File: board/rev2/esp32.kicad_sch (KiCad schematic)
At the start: 3 parts, among them U7 ESP32-C6-WROOM-1

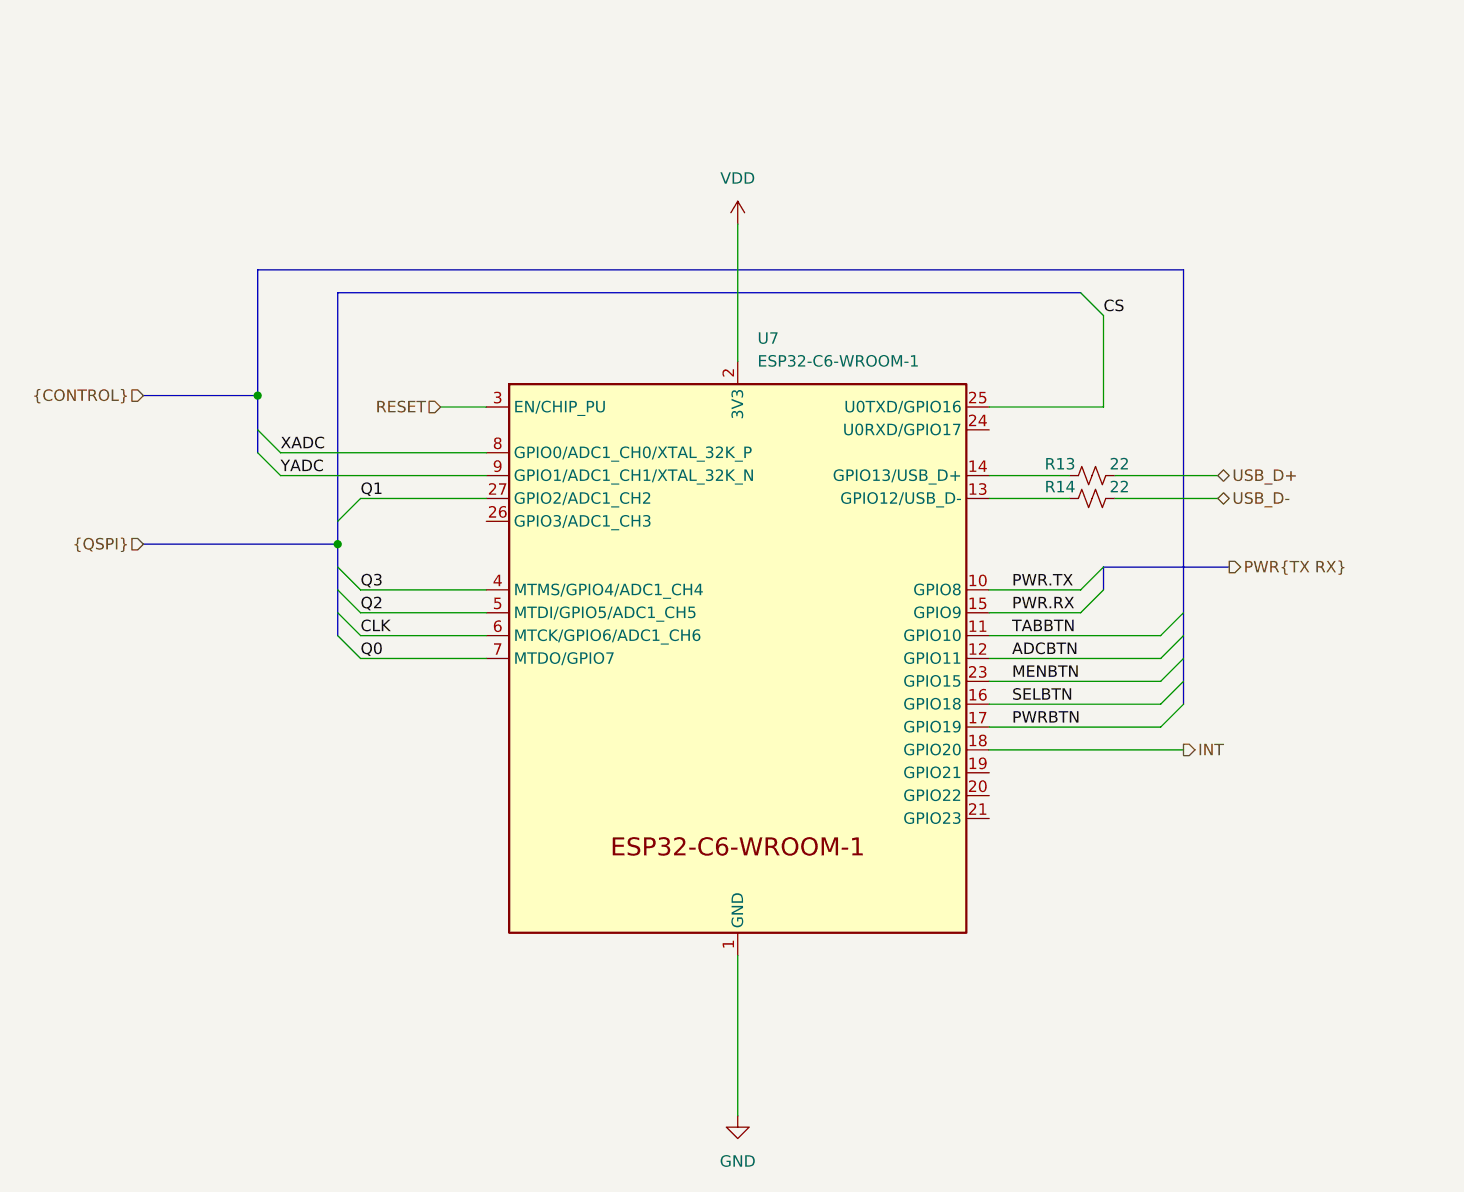
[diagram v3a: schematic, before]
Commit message: Add netclasses, more footprints, fix ERC
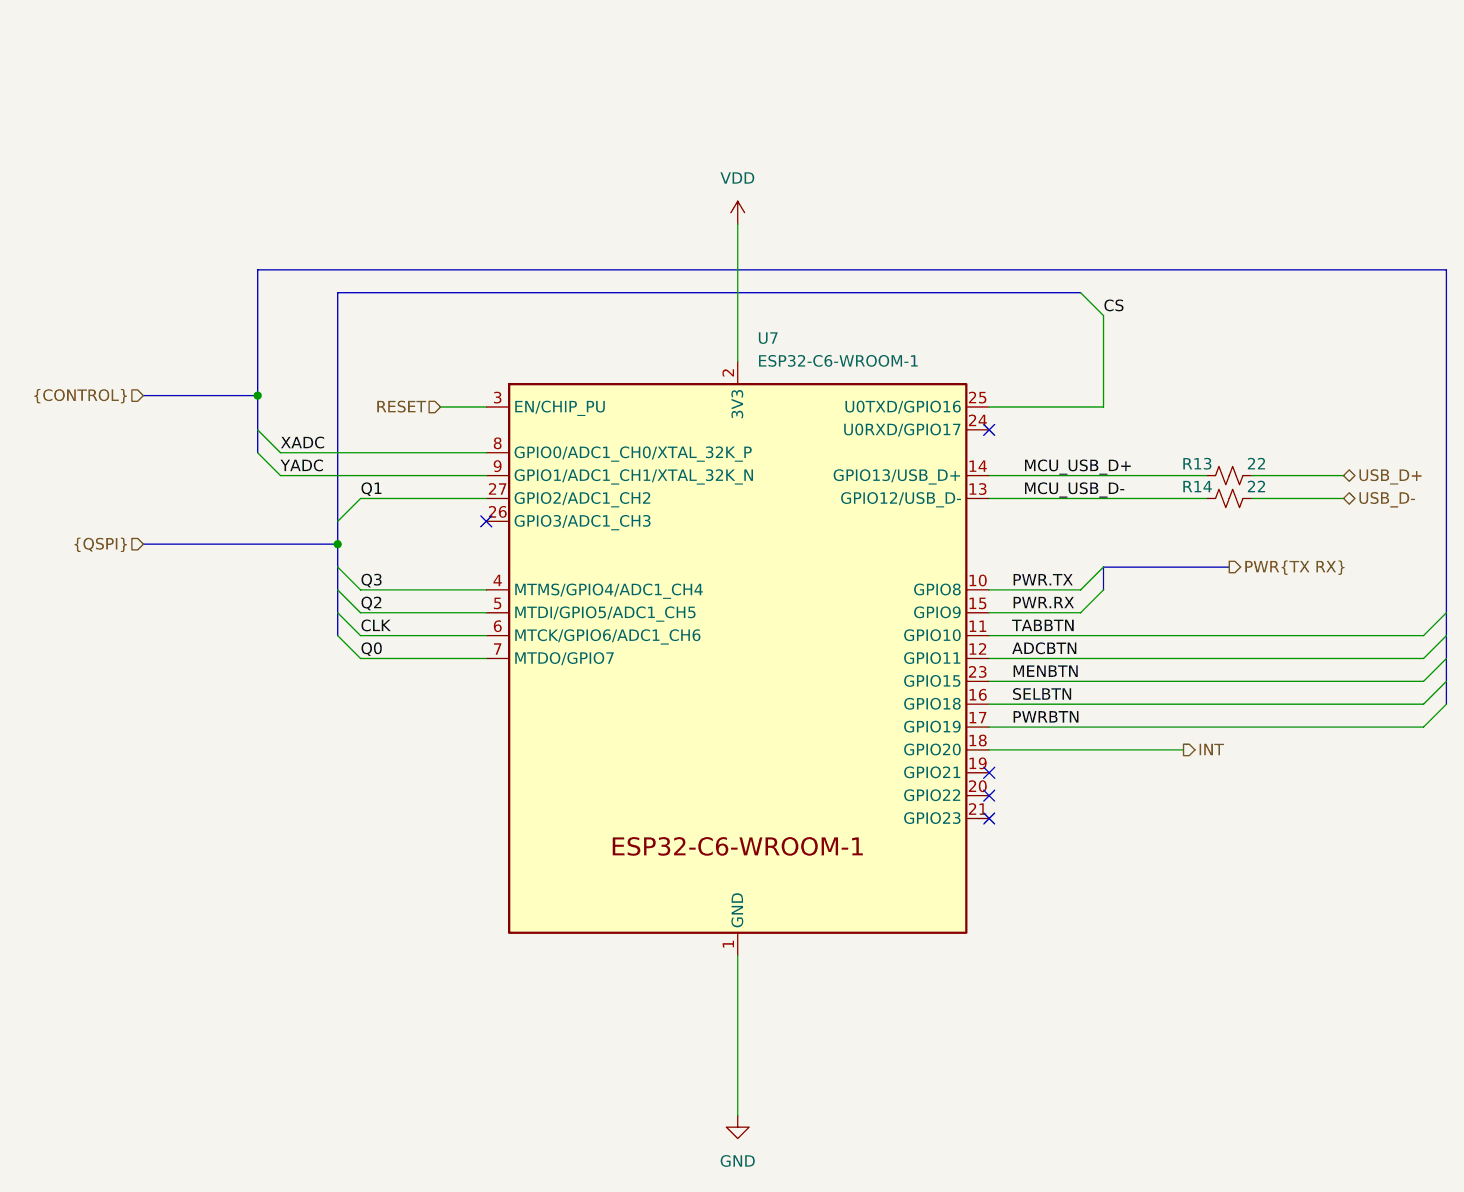
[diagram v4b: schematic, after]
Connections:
- net MCU_USB_D-: now reaches R14.1, U7.13 (GPIO12/USB_D-)
- net MCU_USB_D+: now reaches R13.1, U7.14 (GPIO13/USB_D+)
- no-connect marks 0 -> 5
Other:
- moved on the sheet: R13, R14
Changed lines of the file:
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@@
 		(color 0 0 0 0)
 	)
-	(bus_entry
-		(at 187.96 97.79)
+	(no_connect
+		(at 166.37 67.31)
+	)
+	(no_connect
+		(at 166.37 107.95)
+	)
+	(no_connect
+		(at 166.37 110.49)
+	)
+	(no_connect
+		(at 110.49 77.47)
+	)
+	(no_connect
+		(at 166.37 105.41)
+	)
+	(bus_entry
+		(at 217.17 97.79)
 		(size -2.54 2.54)
 		(stroke
@@
 	)
 	(bus_entry
-		(at 187.96 87.63)
+		(at 217.17 87.63)
 		(size -2.54 2.54)
 		(stroke
@@
 	)
 	(bus_entry
-		(at 187.96 90.17)
+		(at 217.17 90.17)
 		(size -2.54 2.54)
 		(stroke
@@
 	)
 	(bus_entry
-		(at 187.96 95.25)
+		(at 217.17 95.25)
 		(size -2.54 2.54)
 		(stroke
@@
 	)
 	(bus_entry
-		(at 187.96 92.71)
+		(at 217.17 92.71)
 		(size -2.54 2.54)
 		(stroke
@@
 	(wire
 		(pts
-			(xy 166.37 97.79) (xy 185.42 97.79)
+			(xy 166.37 97.79) (xy 214.63 97.79)
 		)
 		(stroke
@@
 	(bus
 		(pts
-			(xy 187.96 95.25) (xy 187.96 97.79)
+			(xy 217.17 95.25) (xy 217.17 97.79)
 		)
 		(stroke
@@
 	(wire
 		(pts
-			(xy 166.37 100.33) (xy 185.42 100.33)
+			(xy 166.37 100.33) (xy 214.63 100.33)
 		)
 		(stroke
@@
 	(wire
 		(pts
-			(xy 166.37 95.25) (xy 185.42 95.25)
-		)
-		(stroke
-			(width 0)
-			(type default)
-		)
-	)
-	(wire
-		(pts
-			(xy 166.37 90.17) (xy 185.42 90.17)
+			(xy 166.37 95.25) (xy 214.63 95.25)
+		)
+		(stroke
+			(width 0)
+			(type default)
+		)
+	)
+	(wire
+		(pts
+			(xy 166.37 90.17) (xy 214.63 90.17)
 		)
 		(stroke
@@
 	(bus
 		(pts
-			(xy 187.96 90.17) (xy 187.96 92.71)
+			(xy 217.17 90.17) (xy 217.17 92.71)
 		)
 		(stroke
@@
 	(wire
 		(pts
-			(xy 166.37 92.71) (xy 185.42 92.71)
-		)
-		(stroke
-			(width 0)
-			(type default)
-		)
-	)
-	(wire
-		(pts
-			(xy 180.34 72.39) (xy 191.77 72.39)
-		)
-		(stroke
-			(width 0)
-			(type default)
-		)
-	)
-	(bus
-		(pts
-			(xy 187.96 87.63) (xy 187.96 90.17)
+			(xy 166.37 92.71) (xy 214.63 92.71)
+		)
+		(stroke
+			(width 0)
+			(type default)
+		)
+	)
+	(wire
+		(pts
+			(xy 195.58 72.39) (xy 205.74 72.39)
+		)
+		(stroke
+			(width 0)
+			(type default)
+		)
+	)
+	(bus
+		(pts
+			(xy 217.17 87.63) (xy 217.17 90.17)
 		)
 		(stroke
@@
 	(bus
 		(pts
-			(xy 187.96 92.71) (xy 187.96 95.25)
+			(xy 217.17 92.71) (xy 217.17 95.25)
 		)
 		(stroke
@@
 	(wire
 		(pts
-			(xy 166.37 72.39) (xy 175.26 72.39)
-		)
-		(stroke
-			(width 0)
-			(type default)
-		)
-	)
-	(bus
-		(pts
-			(xy 85.09 49.53) (xy 187.96 49.53)
-		)
-		(stroke
-			(width 0)
-			(type default)
-		)
-	)
-	(wire
-		(pts
-			(xy 166.37 74.93) (xy 175.26 74.93)
+			(xy 166.37 72.39) (xy 190.5 72.39)
+		)
+		(stroke
+			(width 0)
+			(type default)
+		)
+	)
+	(bus
+		(pts
+			(xy 85.09 49.53) (xy 217.17 49.53)
+		)
+		(stroke
+			(width 0)
+			(type default)
+		)
+	)
+	(wire
+		(pts
+			(xy 166.37 74.93) (xy 190.5 74.93)
 		)
 		(stroke
@@
 	(bus
 		(pts
-			(xy 187.96 49.53) (xy 187.96 87.63)
+			(xy 217.17 49.53) (xy 217.17 87.63)
 		)
 		(stroke
@@
 	(wire
 		(pts
-			(xy 180.34 74.93) (xy 191.77 74.93)
+			(xy 195.58 74.93) (xy 205.74 74.93)
 		)
 		(stroke
@@
 		)
 	)
+	(label "MCU_USB_D+"
+		(at 170.18 72.39 0)
+		(effects
+			(font
+				(size 1.27 1.27)
+			)
+			(justify left bottom)
+		)
+	)
+	(label "MCU_USB_D-"
+		(at 170.18 74.93 0)
+		(effects
+			(font
+				(size 1.27 1.27)
+			)
+			(justify left bottom)
+		)
+	)
 	(label "Q2"
 		(at 96.52 87.63 0)
@@
 	(hierarchical_label "USB_D+"
 		(shape bidirectional)
-		(at 191.77 72.39 0)
+		(at 205.74 72.39 0)
 		(effects
 			(font
@@
 	(hierarchical_label "USB_D-"
 		(shape bidirectional)
-		(at 191.77 74.93 0)
+		(at 205.74 74.93 0)
 		(effects
 			(font
@@
 			)
 			(justify right)
+		)
+	)
+	(rule_area
+		(polyline
+			(pts
+				(xy 168.91 68.58) (xy 201.93 68.58) (xy 201.93 77.47) (xy 168.91 77.47)
+			)
+			(stroke
+				(width 0)
+				(type dash)
+			)
+			(fill
+				(type none)
+			)
+		)
+	)
+	(netclass_flag ""
+		(length 2.54)
+		(shape round)
+		(at 187.96 68.58 0)
+		(fields_autoplaced yes)
+		(effects
+			(font
+				(size 1.27 1.27)
+			)
+			(justify left bottom)
+		)
+		(property "Netclass" "USB"
+			(at 188.6585 66.04 0)
+			(effects
+				(font
+					(size 1.27 1.27)
+				)
+				(justify left)
+			)
+		)
+		(property "Component Class" ""
+			(at -34.29 -2.54 0)
+			(effects
+				(font
+					(size 1.27 1.27)
+					(italic yes)
+				)
+			)
 		)
 	)
@@
 	(symbol
 		(lib_id "Device:R_Small_US")
-		(at 177.8 74.93 90)
+		(at 193.04 74.93 90)
 		(unit 1)
 		(exclude_from_sim no)
@@
 		(dnp no)
 		(property "Reference" "R14"
-			(at 174.244 73.66 90)
+			(at 189.484 73.66 90)
 			(effects
 				(font
@@
 		)
 		(property "Value" "22"
-			(at 180.848 73.66 90)
+			(at 196.088 73.66 90)
 			(effects
 				(font
@@
 		)
 		(property "Footprint" "Resistor_SMD:R_0402_1005Metric"
-			(at 177.8 74.93 0)
+			(at 193.04 74.93 0)
 			(effects
 				(font
@@
 		)
 		(property "Datasheet" "~"
-			(at 177.8 74.93 0)
+			(at 193.04 74.93 0)
 			(effects
 				(font
@@
 		)
 		(property "Description" "Resistor, small US symbol"
-			(at 177.8 74.93 0)
+			(at 193.04 74.93 0)
 			(effects
 				(font
@@
 		)
 		(property "Part" " 0402WGF220JTCE"
-			(at 177.8 74.93 90)
+			(at 193.04 74.93 90)
 			(effects
 				(font
@@
 	(symbol
 		(lib_id "Device:R_Small_US")
-		(at 177.8 72.39 90)
+		(at 193.04 72.39 90)
 		(unit 1)
 		(exclude_from_sim no)
@@
 		(dnp no)
 		(property "Reference" "R13"
-			(at 174.244 71.12 90)
+			(at 189.484 71.12 90)
 			(effects
 				(font
@@
 		)
 		(property "Value" "22"
-			(at 180.848 71.12 90)
+			(at 196.088 71.12 90)
 			(effects
 				(font
@@
 		)
 		(property "Footprint" "Resistor_SMD:R_0402_1005Metric"
-			(at 177.8 72.39 0)
+			(at 193.04 72.39 0)
 			(effects
 				(font
@@
 		)
 		(property "Datasheet" "~"
-			(at 177.8 72.39 0)
+			(at 193.04 72.39 0)
 			(effects
 				(font
@@
 		)
 		(property "Description" "Resistor, small US symbol"
-			(at 177.8 72.39 0)
+			(at 193.04 72.39 0)
 			(effects
 				(font
@@
 		)
 		(property "Part" " 0402WGF220JTCE"
-			(at 177.8 72.39 90)
-			(effects
-				(font
+			(at 193.04 72.39 90)
+			(effects
+				(font

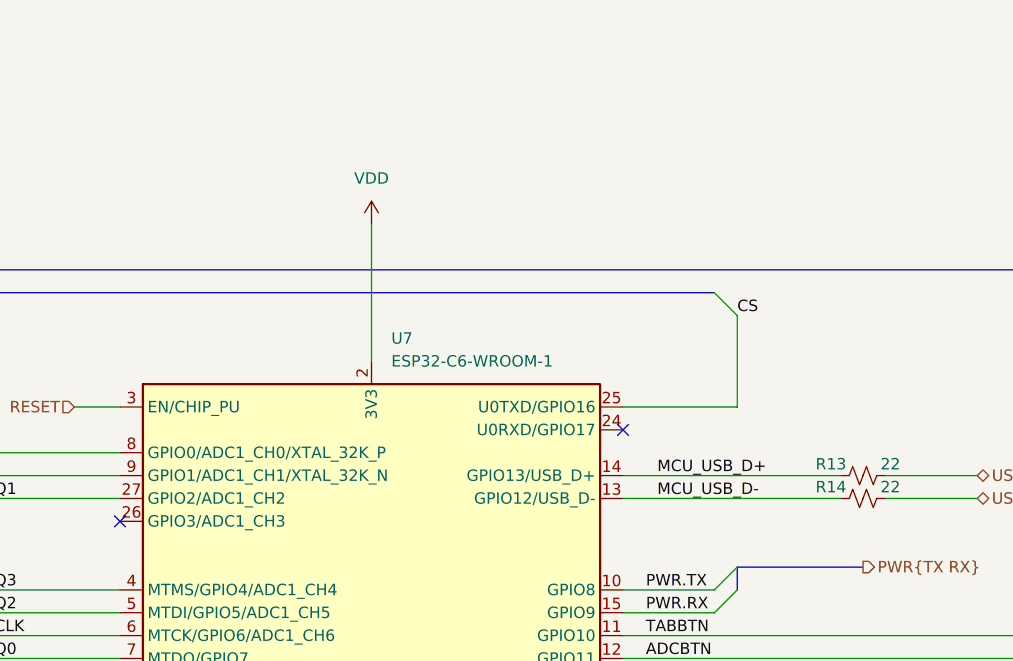
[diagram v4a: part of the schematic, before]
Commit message: Really finish rev2 board schematic
- fix some more footprints
  - move to real SD card holder, for example
- repair part numbers
- add LCSC part refs to everything
- add even more caps to the 3.3V reg output
  - really should use an LDO but meh it should be fine

total BOM cost for 5 of them is apparently 160 CAD, or like 32 dollars
each (don't think that includes the feeder fees tho)
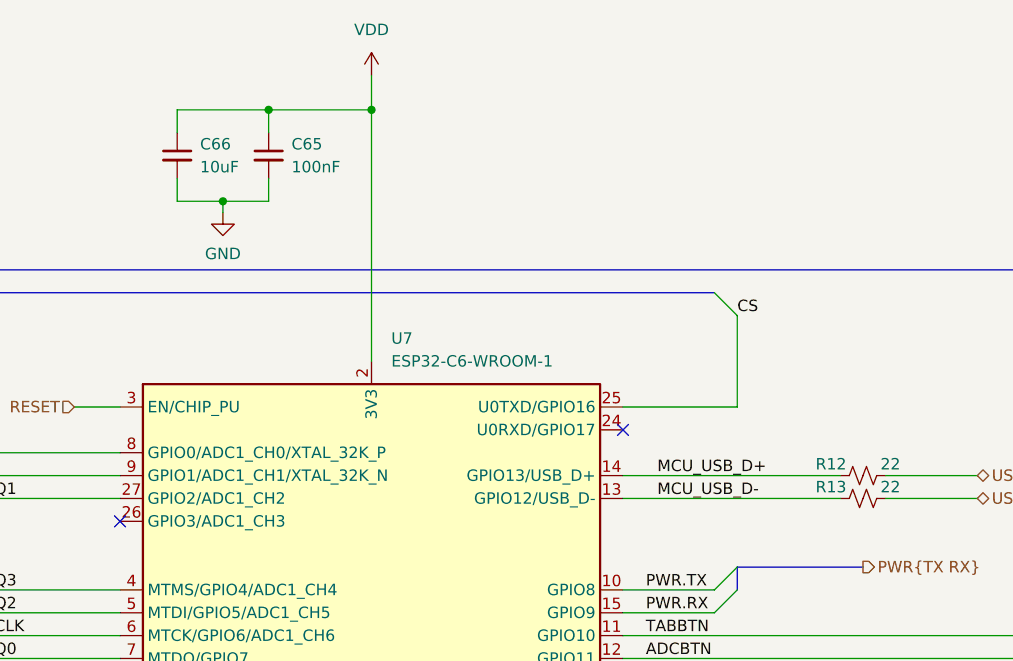
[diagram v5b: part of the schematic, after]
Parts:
- added C65: 100nF, Capacitor_SMD:C_0402_1005Metric, symbol Device:C_Small
- added C66: 10uF, Capacitor_SMD:C_1210_3225Metric, symbol Device:C_Small
- R12: renamed from R13; LCSC (none) -> C25092
- R13: renamed from R14; LCSC (none) -> C25092
- U7: LCSC (none) -> C5366877; Part ESP32-C6-WROOM-1 -> ESP32-C6-WROOM-1-N8
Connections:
- net GND: now also C65.2, C66.2
- net VDD: now also C65.1, C66.1

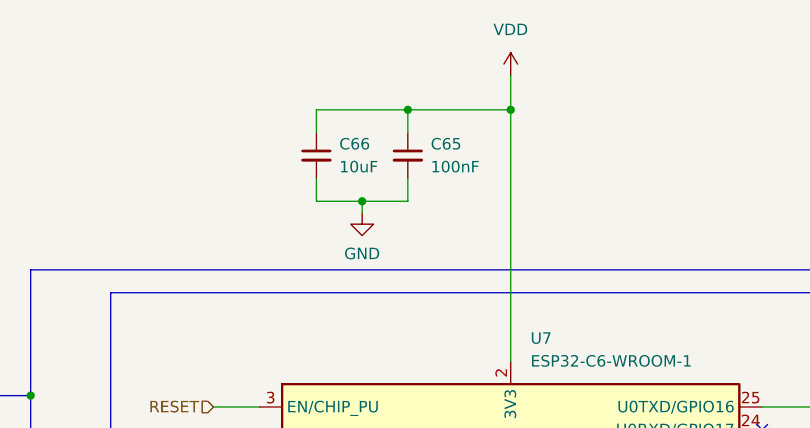
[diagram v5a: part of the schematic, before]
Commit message: Start board
add a few extra bypass caps too, and swap some pins on the USB mux

i forgot to add a bypass cap on the tpd6s so that also needs to happen

truly 63 capacitors is not enough
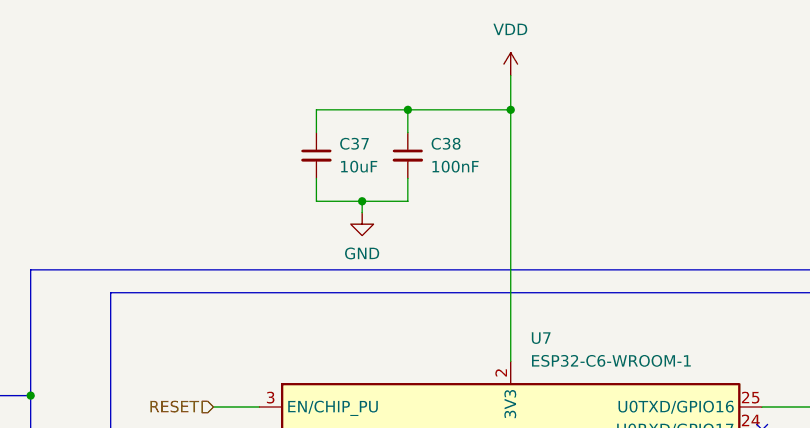
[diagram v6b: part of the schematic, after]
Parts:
- renumbered C66 to C37, C65 to C38
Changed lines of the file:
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@@
 		(dnp no)
 		(fields_autoplaced yes)
-		(property "Reference" "#PWR018"
+		(property "Reference" "#PWR019"
 			(at 138.43 31.75 0)
 			(effects
@@
 			(project "mainboard"
 				(path "/32eb05c7-b4a6-42f3-8fb3-43453631100f/ab8e590b-cde3-4860-87b4-37e60f787bc4"
-					(reference "#PWR018")
+					(reference "#PWR019")
 					(unit 1)
 				)
@@
 		(on_board yes)
 		(dnp no)
-		(property "Reference" "#PWR063"
+		(property "Reference" "#PWR018"
 			(at 121.92 49.53 0)
 			(effects
@@
 			(project "mainboard"
 				(path "/32eb05c7-b4a6-42f3-8fb3-43453631100f/ab8e590b-cde3-4860-87b4-37e60f787bc4"
-					(reference "#PWR063")
+					(reference "#PWR018")
 					(unit 1)
 				)
@@
 		(dnp no)
 		(fields_autoplaced yes)
-		(property "Reference" "C65"
+		(property "Reference" "C38"
 			(at 129.54 35.5662 0)
 			(effects
@@
 			(project "mainboard"
 				(path "/32eb05c7-b4a6-42f3-8fb3-43453631100f/ab8e590b-cde3-4860-87b4-37e60f787bc4"
-					(reference "C65")
+					(reference "C38")
 					(unit 1)
 				)
@@
 		(dnp no)
 		(fields_autoplaced yes)
-		(property "Reference" "C66"
+		(property "Reference" "C37"
 			(at 119.38 35.5662 0)
 			(effects
@@
 			(project "mainboard"
 				(path "/32eb05c7-b4a6-42f3-8fb3-43453631100f/ab8e590b-cde3-4860-87b4-37e60f787bc4"
-					(reference "C66")
+					(reference "C37")
 					(unit 1)
 				)
@@
 		(dnp no)
 		(fields_autoplaced yes)
-		(property "Reference" "#PWR019"
+		(property "Reference" "#PWR020"
 			(at 138.43 149.86 0)
 			(effects
@@
 			(project "mainboard"
 				(path "/32eb05c7-b4a6-42f3-8fb3-43453631100f/ab8e590b-cde3-4860-87b4-37e60f787bc4"
-					(reference "#PWR019")
-					(unit 1)
-				)
+					(reference "#PWR020")
+					(unit 1)
+				)

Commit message: Finish board rev2
woo another pcb
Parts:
- C37: footprint Capacitor_SMD:C_1210_3225Metric -> Capacitor_SMD:C_1206_3216Metric
